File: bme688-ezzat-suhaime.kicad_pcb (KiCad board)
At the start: 4 copper layers, 30 x 20 mm, 21 parts, among them J1 Conn_01x07, J2 STEMMA_I2C_QT, J3 STEMMA_I2C_QT, Q1 BSS138BKS,115, U1 BME688, U2 XC6210B332MR-G

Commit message: Adding pcb stacking stripes
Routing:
- added copper zone on In1.Cu, net (none)
- added copper zone on In2.Cu, net (none)
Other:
- board text added: "2"
- board text added: "3"
- board text added: "BME688"
- board text removed: "ezzat"
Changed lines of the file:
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@@
 		(layer "Edge.Cuts")
 	)
-	(gr_text "ezzat"
-		(at 216.5 104.5 0)
+	(gr_text "2"
+		(at 239.75 98.5 0)
+		(layer "In1.Cu")
+		(effects
+			(font
+				(size 1 1)
+				(thickness 0.25)
+				(bold yes)
+			)
+			(justify left bottom)
+		)
+	)
+	(gr_text "3"
+		(at 241 96 0)
+		(layer "In2.Cu")
+		(effects
+			(font
+				(size 1 1)
+				(thickness 0.25)
+				(bold yes)
+			)
+			(justify left bottom mirror)
+		)
+	)
+	(gr_text "catbranchman"
+		(at 216.25 106.25 0)
 		(layer "F.SilkS")
 		(effects
@@
 				(size 0.8 0.5)
 				(thickness 0.09375)
+				(bold yes)
+			)
+			(justify left bottom)
+		)
+	)
+	(gr_text "BME688"
+		(at 216.25 105.25 0)
+		(layer "F.SilkS")
+		(effects
+			(font
+				(size 1 0.5)
+				(thickness 0.125)
 				(bold yes)
 			)
@@
 		)
 	)
-	(gr_text "catbranchman"
-		(at 216.5 103.5 0)
-		(layer "F.SilkS")
-		(effects
-			(font
-				(size 1 0.6)
-				(thickness 0.125)
-				(bold yes)
-			)
-			(justify left bottom)
-		)
-	)
 	(gr_text "SDI"
 		(at 231.5 88.25 0)
@@
 	)
 	(segment
+		(start 224.7952 96.5)
+		(end 223.65 96.5)
+		(width 0.5)
+		(layer "F.Cu")
+		(net 1)
+	)
+	(segment
 		(start 236.625 98.5)
 		(end 239.2 98.5)
@@
 	)
 	(segment
+		(start 223.65 96.5)
+		(end 223.5625 96.4125)
+		(width 0.5)
+		(layer "F.Cu")
+		(net 1)
+	)
+	(segment
 		(start 239.2 98.5)
 		(end 240.5 99.8)
@@
 	)
 	(segment
-		(start 224.7952 97)
-		(end 224.15 97)
-		(width 0.5)
-		(layer "F.Cu")
-		(net 1)
-	)
-	(segment
-		(start 224.15 97)
-		(end 223.5625 96.4125)
-		(width 0.5)
-		(layer "F.Cu")
-		(net 1)
-	)
-	(segment
 		(start 227.25 97.975)
 		(end 226.5 97.975)
@@
 	)
 	(via
-		(at 224.7952 97)
+		(at 224.7952 96.5)
 		(size 0.8)
 		(drill 0.4)
@@
 			)
 		)
+	)
+	(zone
+		(net 0)
+		(net_name "")
+		(layer "In1.Cu")
+		(hatch edge 0.5)
+		(priority 2)
+		(connect_pads
+			(clearance 0.508)
+		)
+		(min_thickness 0.25)
+		(filled_areas_thickness no)
+		(fill
+			(mode hatch)
+			(thermal_gap 0.5)
+			(thermal_bridge_width 0.5)
+			(island_removal_mode 1)
+			(island_area_min 10)
+			(hatch_thickness 1)
+			(hatch_gap 1.5)
+			(hatch_orientation 0)
+			(hatch_border_algorithm hatch_thickness)
+			(hatch_min_hole_area 0.3)
+		)
+		(polygon
+			(pts
+				(xy 242 99) (xy 239 99) (xy 239 96.75) (xy 242 96.75)
+			)
+		)
+	)
+	(zone
+		(net 0)
+		(net_name "")
+		(layer "In2.Cu")
+		(hatch edge 0.5)
+		(priority 3)
+		(connect_pads
+			(clearance 0.508)
+		)
+		(min_thickness 0.25)
+		(filled_areas_thickness no)
+		(fill
+			(mode hatch)
+			(thermal_gap 0.5)
+			(thermal_bridge_width 0.5)
+			(island_removal_mode 1)
+			(island_area_min 10)
+			(hatch_thickness 1)
+			(hatch_gap 1.5)
+			(hatch_orientation 0)
+			(hatch_border_algorithm hatch_thickness)
+			(hatch_min_hole_area 0.3)
+		)
+		(polygon
+			(pts
+				(xy 239 99) (xy 239 94.75) (xy 241.75 94.75) (xy 241.75 99)
+			)
+		)

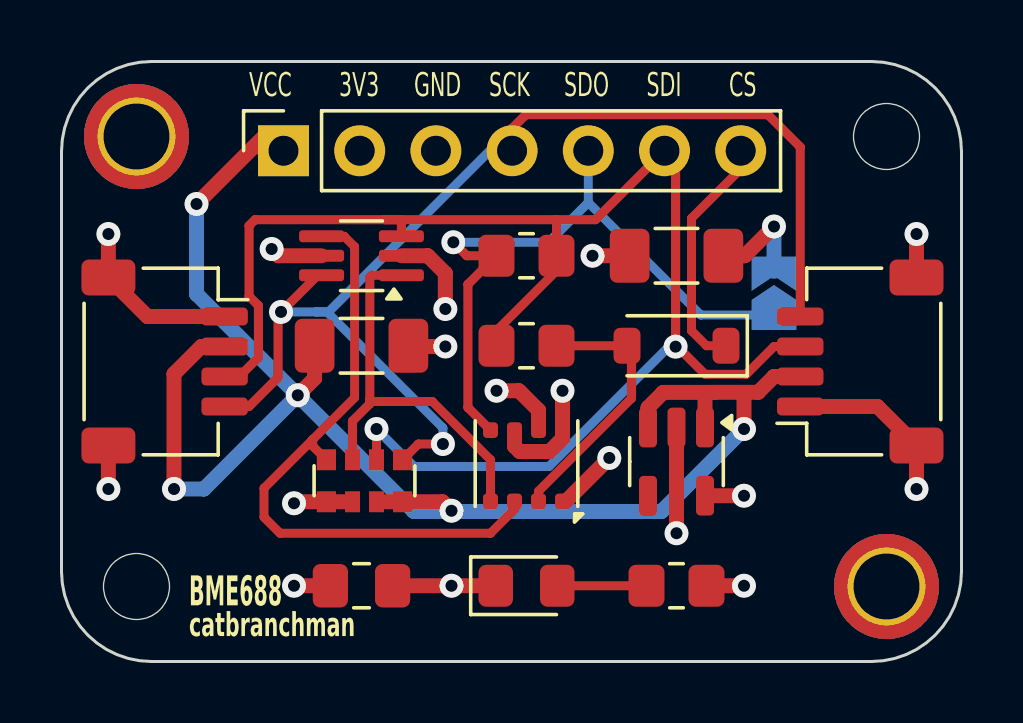
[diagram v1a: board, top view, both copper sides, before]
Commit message: Fixes per Steve & Brian
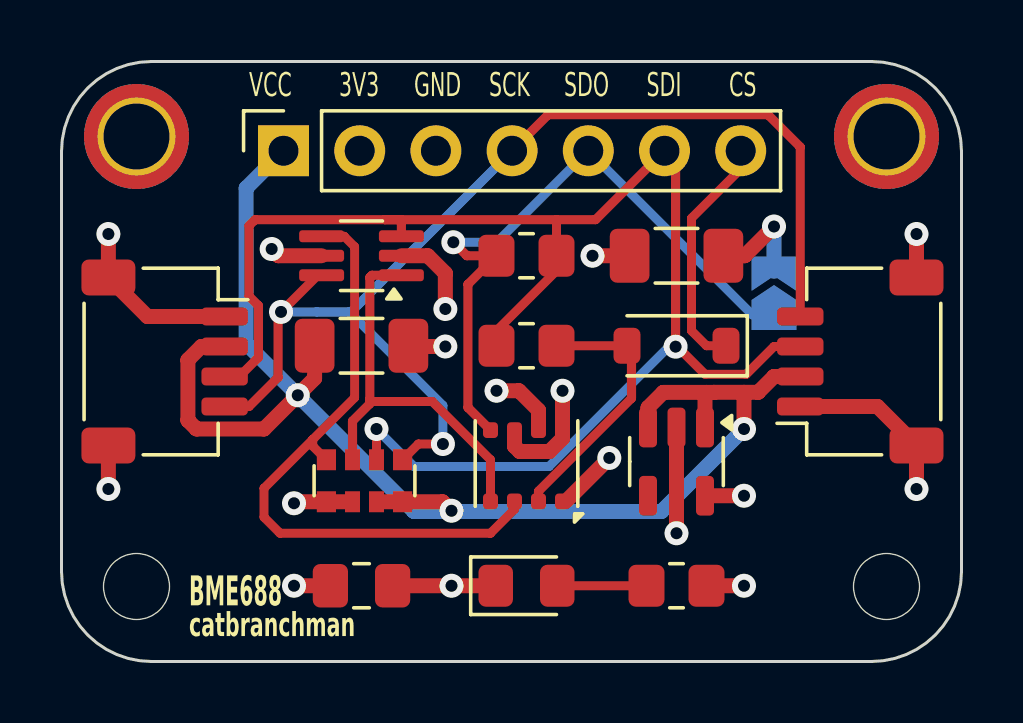
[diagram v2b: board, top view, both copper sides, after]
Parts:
- moved H2 15.0 mm to (239.5, 89.5)
- moved H4 15.0 mm to (239.5, 104.5)
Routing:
- net VCC: track 53.8 -> 48.1 mm, vias 5 -> 3
- removed copper zone on In1.Cu, net (none)
- removed copper zone on In2.Cu, net (none)
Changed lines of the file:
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@@
 	(footprint "MountingHole:MountingHole_2.2mm_M2_ISO7380"
 		(layer "F.Cu")
-		(at 239.5 89.5)
+		(at 239.5 104.5)
 		(descr "Mounting Hole 2.2mm, no annular, M2, ISO7380")
 		(tags "mounting hole 2.2mm no annular m2 iso7380")
@@
 	(footprint "MountingHole:MountingHole_2.2mm_M2_ISO7380_Pad_TopBottom"
 		(layer "F.Cu")
-		(at 239.5 104.5)
+		(at 239.5 89.5)
 		(descr "Mounting Hole 2.2mm, M2, ISO7380")
 		(tags "mounting hole 2.2mm m2 iso7380")
@@
 	)
 	(gr_text "2"
-		(at 239.75 98.5 0)
+		(at 239.75 98.75 0)
 		(layer "In1.Cu")
 		(effects
@@
 	)
 	(gr_text "3"
-		(at 241 96 0)
+		(at 241 96.25 0)
 		(layer "In2.Cu")
 		(effects
@@
 	)
 	(segment
-		(start 223.65 96.5)
-		(end 223.5625 96.4125)
-		(width 0.5)
-		(layer "F.Cu")
-		(net 1)
-	)
-	(segment
 		(start 239.2 98.5)
 		(end 240.5 99.8)
@@
 	)
 	(segment
+		(start 217.4375 96.5)
+		(end 216.662501 96.5)
+		(width 0.5)
+		(layer "F.Cu")
+		(net 2)
+	)
+	(segment
 		(start 225 101.975)
 		(end 224.7 101.675)
@@
 	)
 	(segment
-		(start 234.75 98.0274)
-		(end 233.75 98.0274)
+		(start 216.2125 98.9625)
+		(end 216.5 99.25)
 		(width 0.5)
 		(layer "F.Cu")
@@
 	)
 	(segment
-		(start 232.057701 98.0298)
-		(end 231.55 98.537501)
+		(start 234.75 98.0274)
+		(end 233.75 98.0274)
 		(width 0.5)
 		(layer "F.Cu")
@@
 	)
 	(segment
-		(start 215.75 101.25)
-		(end 215.75 97.412501)
+		(start 232.057701 98.0298)
+		(end 231.55 98.537501)
 		(width 0.5)
 		(layer "F.Cu")
@@
 	)
 	(segment
-		(start 219.4 89.975)
-		(end 218.75 89.975)
+		(start 216.5 99.25)
+		(end 218.75 99.25)
 		(width 0.5)
 		(layer "F.Cu")
@@
 	)
 	(segment
-		(start 218.75 89.5)
-		(end 216.5 91.75)
-		(width 0.5)
-		(layer "F.Cu")
-		(net 2)
-	)
-	(segment
 		(start 223.37 101.675)
 		(end 222.5 101.675)
@@
 	)
 	(segment
-		(start 215.75 97.412501)
-		(end 216.662501 96.5)
+		(start 231.55 98.537501)
+		(end 231.55 99.2)
 		(width 0.5)
 		(layer "F.Cu")
@@
 	(segment
 		(start 216.662501 96.5)
-		(end 217.4375 96.5)
+		(end 216.2125 96.950001)
 		(width 0.5)
 		(layer "F.Cu")
@@
 	)
 	(segment
-		(start 231.55 98.537501)
-		(end 231.55 99.2)
+		(start 216.2125 96.950001)
+		(end 216.2125 98.9625)
 		(width 0.5)
 		(layer "F.Cu")
@@
 	)
 	(segment
+		(start 218.75 99.25)
+		(end 219.875 98.125)
+		(width 0.5)
+		(layer "F.Cu")
+		(net 2)
+	)
+	(segment
 		(start 233.7476 98.0298)
 		(end 233.5 98.0298)
@@
 	)
 	(via
-		(at 216.5 91.75)
-		(size 0.8)
-		(drill 0.4)
-		(layers "F.Cu" "B.Cu")
-		(net 2)
-	)
-	(via
 		(at 234.75 99.25)
 		(size 0.8)
@@
 	)
 	(via
-		(at 215.75 101.25)
-		(size 0.8)
-		(drill 0.4)
-		(layers "F.Cu" "B.Cu")
-		(net 2)
-	)
-	(via
 		(at 219.875 98.125)
 		(size 0.8)
@@
 	)
 	(segment
-		(start 223.75 102)
-		(end 232 102)
-		(width 0.5)
-		(layer "B.Cu")
-		(net 2)
-	)
-	(segment
-		(start 219.782935 98.029172)
-		(end 219.779172 98.029172)
+		(start 219.875 98.125)
+		(end 218.1548 96.4048)
 		(width 0.5)
 		(layer "B.Cu")
@@
 	)
 	(segment
-		(start 216.75 101.25)
-		(end 219.782935 98.217065)
+		(start 223.75 102)
+		(end 232 102)
 		(width 0.5)
 		(layer "B.Cu")
@@
 	)
 	(segment
-		(start 215.75 101.25)
-		(end 216.75 101.25)
+		(start 218.1548 96.4048)
+		(end 218.1548 91.2202)
 		(width 0.5)
 		(layer "B.Cu")
@@
 	)
 	(segment
-		(start 219.779172 98.029172)
-		(end 216.5 94.75)
+		(start 218.1548 91.2202)
+		(end 219.4 89.975)
 		(width 0.5)
 		(layer "B.Cu")
@@
 	)
 	(segment
-		(start 216.5 94.75)
-		(end 216.5 91.75)
-		(width 0.5)
-		(layer "B.Cu")
-		(net 2)
-	)
-	(segment
 		(start 228.7 97.975)
 		(end 228.7 99.2875)
@@
 	)
 	(segment
-		(start 235.5476 88.7726)
-		(end 227.4774 88.7726)
+		(start 228.2224 88.7726)
+		(end 227.02 89.975)
 		(width 0.3048)
 		(layer "F.Cu")
@@
 	)
 	(segment
-		(start 224.714341 99.75)
-		(end 223.895 99.75)
-		(width 0.3)
+		(start 235.5476 88.7726)
+		(end 228.2224 88.7726)
+		(width 0.3048)
 		(layer "F.Cu")
 		(net 14)
 	)
 	(segment
-		(start 236.625 89.85)
-		(end 235.5476 88.7726)
-		(width 0.3048)
+		(start 224.714341 99.75)
+		(end 223.895 99.75)
+		(width 0.3)
 		(layer "F.Cu")
 		(net 14)
@@
 	)
 	(segment
-		(start 227.4774 88.7726)
-		(end 227.02 89.23)
-		(width 0.3048)
-		(layer "F.Cu")
-		(net 14)
-	)
-	(segment
-		(start 227.02 89.23)
-		(end 227.02 89.975)
+		(start 236.625 89.85)
+		(end 235.5476 88.7726)
 		(width 0.3048)
 		(layer "F.Cu")
@@
 	)
 	(segment
-		(start 220.5 95.3476)
-		(end 220.9024 95.3476)
+		(start 221.6524 95.3476)
+		(end 226.75 90.25)
 		(width 0.3048)
 		(layer "B.Cu")
@@
 	)
 	(segment
-		(start 220.9024 95.3476)
-		(end 226.75 89.5)
-		(width 0.3048)
+		(start 224.714341 98.464341)
+		(end 221.5976 95.3476)
+		(width 0.3)
 		(layer "B.Cu")
 		(net 14)
 	)
 	(segment
-		(start 224.714341 99.75)
-		(end 224.714341 99.214341)
+		(start 221.5976 95.3476)
+		(end 220.5 95.3476)
 		(width 0.3)
 		(layer "B.Cu")
@@
 	)
 	(segment
-		(start 220.5 95.3476)
-		(end 219.3173 95.3476)
-		(width 0.3048)
+		(start 224.714341 99.75)
+		(end 224.714341 98.464341)
+		(width 0.3)
 		(layer "B.Cu")
 		(net 14)
 	)
 	(segment
-		(start 224.714341 99.214341)
-		(end 220.8476 95.3476)
-		(width 0.3)
+		(start 220.5 95.3476)
+		(end 221.6524 95.3476)
+		(width 0.3048)
 		(layer "B.Cu")
 		(net 14)
 	)
 	(segment
-		(start 220.8476 95.3476)
-		(end 220.5 95.3476)
-		(width 0.3)
+		(start 220.5 95.3476)
+		(end 219.3173 95.3476)
+		(width 0.3048)
 		(layer "B.Cu")
 		(net 14)
@@
 	)
 	(segment
-		(start 229.56 91.7025)
-		(end 233.3075 95.45)
+		(start 229.56 89.975)
+		(end 235.035 95.45)
 		(width 0.3)
 		(layer "B.Cu")
@@
 	)
 	(segment
-		(start 228.25 93.0125)
-		(end 229.56 91.7025)
-		(width 0.3)
-		(layer "B.Cu")
-		(net 15)
-	)
-	(segment
-		(start 233.3075 95.45)
-		(end 235.75 95.45)
+		(start 225.061139 93.025)
+		(end 226.51 93.025)
 		(width 0.3)
 		(layer "B.Cu")
@@
 	)
 	(segment
-		(start 225.061139 93.025)
-		(end 228.25 93.025)
+		(start 226.51 93.025)
+		(end 229.56 89.975)
 		(width 0.3)
 		(layer "B.Cu")
@@
 	)
 	(segment
-		(start 229.56 91.7025)
-		(end 229.56 89.975)
+		(start 235.035 95.45)
+		(end 235.75 95.45)
 		(width 0.3)
 		(layer "B.Cu")
@@
 		(layer "In1.Cu")
 		(hatch edge 0.5)
-		(priority 2)
 		(connect_pads
-			(clearance 0.508)
+			(clearance 0)
 		)
 		(min_thickness 0.25)
 		(filled_areas_thickness no)
+		(keepout
+			(tracks not_allowed)
+			(vias not_allowed)
+			(pads not_allowed)
+			(copperpour not_allowed)
+			(footprints allowed)
+		)
 		(fill
-			(mode hatch)
 			(thermal_gap 0.5)
 			(thermal_bridge_width 0.5)
-			(island_removal_mode 1)
-			(island_area_min 10)
-			(hatch_thickness 1)
-			(hatch_gap 1.5)
-			(hatch_orientation 0)
-			(hatch_border_algorithm hatch_thickness)
-			(hatch_min_hole_area 0.3)
 		)
 		(polygon
 			(pts
-				(xy 242 99) (xy 239 99) (xy 239 96.75) (xy 242 96.75)
+				(xy 242.5 99.5) (xy 238.5 99.5) (xy 238.5 97) (xy 242.5 97)
 			)
 		)
 	)
 	(zone
-		(net 0)
-		(net_name "")
+		(net 3)
+		(net_name "+3.3V")
 		(layer "In2.Cu")
 		(hatch edge 0.5)
-		(priority 3)
+		(priority 1)
 		(connect_pads
 			(clearance 0.508)
@@
 		(min_thickness 0.25)
 		(filled_areas_thickness no)
-		(fill
-			(mode hatch)
+		(fill yes
 			(thermal_gap 0.5)
 			(thermal_bridge_width 0.5)
-			(island_removal_mode 1)
-			(island_area_min 10)
-			(hatch_thickness 1)
-			(hatch_gap 1.5)
-			(hatch_orientation 0)
-			(hatch_border_algorithm hatch_thickness)
-			(hatch_min_hole_area 0.3)
 		)
 		(polygon
 			(pts
-				(xy 239 99) (xy 239 94.75) (xy 241.75 94.75) (xy 241.75 99)
+				(xy 209 114.5) (xy 209 84) (xy 248.5 84.5) (xy 248 114)
 			)
 		)
 	)
 	(zone
-		(net 3)
-		(net_name "+3.3V")
+		(net 0)
+		(net_name "")
 		(layer "In2.Cu")
 		(hatch edge 0.5)
-		(priority 1)
 		(connect_pads
-			(clearance 0.508)
+			(clearance 0)
 		)
 		(min_thickness 0.25)
 		(filled_areas_thickness no)
-		(fill yes
+		(keepout
+			(tracks not_allowed)
+			(vias not_allowed)
+			(pads not_allowed)
+			(copperpour not_allowed)
+			(footprints allowed)
+		)
+		(fill
 			(thermal_gap 0.5)
 			(thermal_bridge_width 0.5)
@@
 		(polygon
 			(pts
-				(xy 209 114.5) (xy 209 84) (xy 248.5 84.5) (xy 248 114)
+				(xy 242.5 99.5) (xy 238.5 99.5) (xy 238.5 94.25) (xy 242.5 94.25)
 			)
 		)
